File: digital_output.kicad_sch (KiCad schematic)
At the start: 11 parts, among them J4 Conn_01x04_Pin, Q1 NMOS, Q13 PMOS, Q2 NMOS, Q9 PMOS

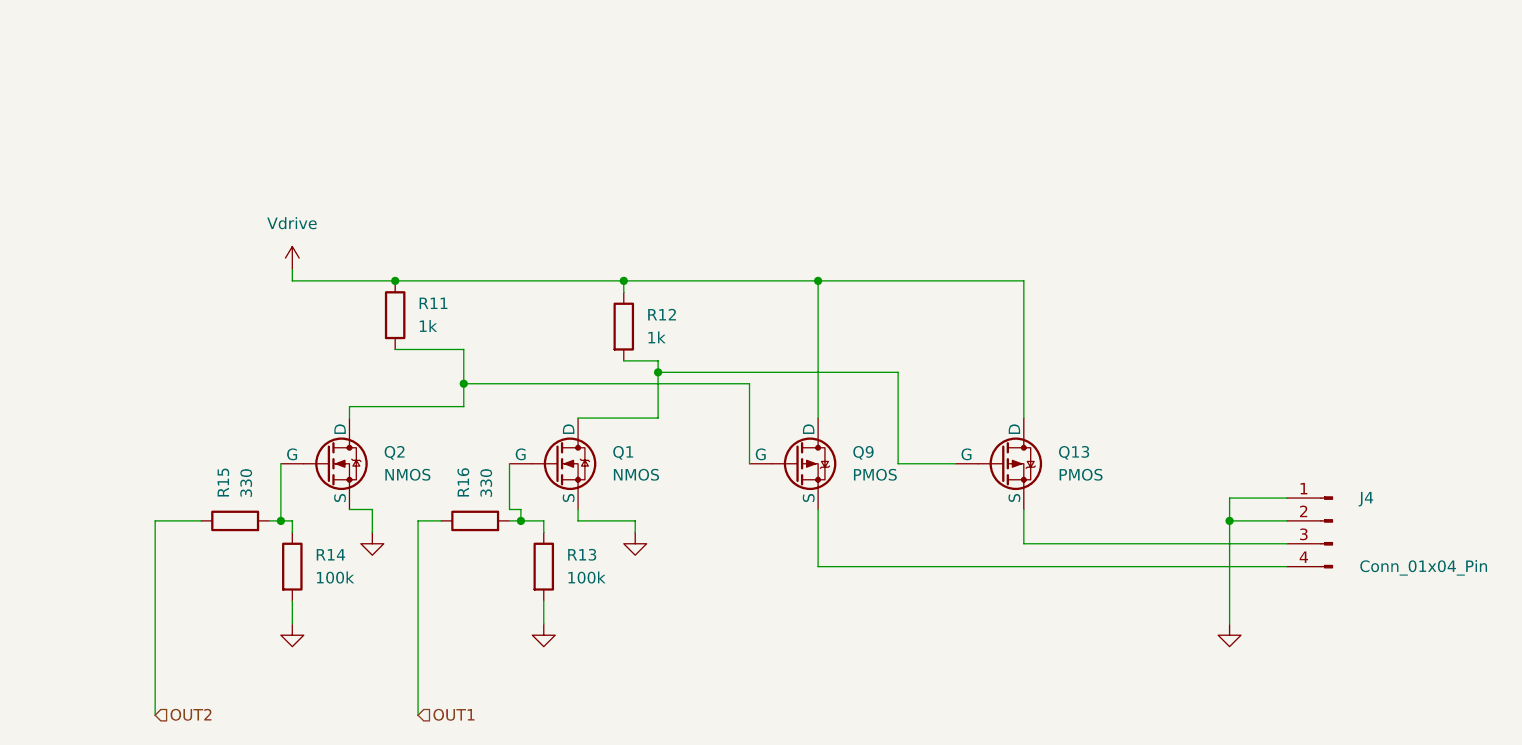
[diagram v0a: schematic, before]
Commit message: cleanup/commenting for better readability, minor corrections
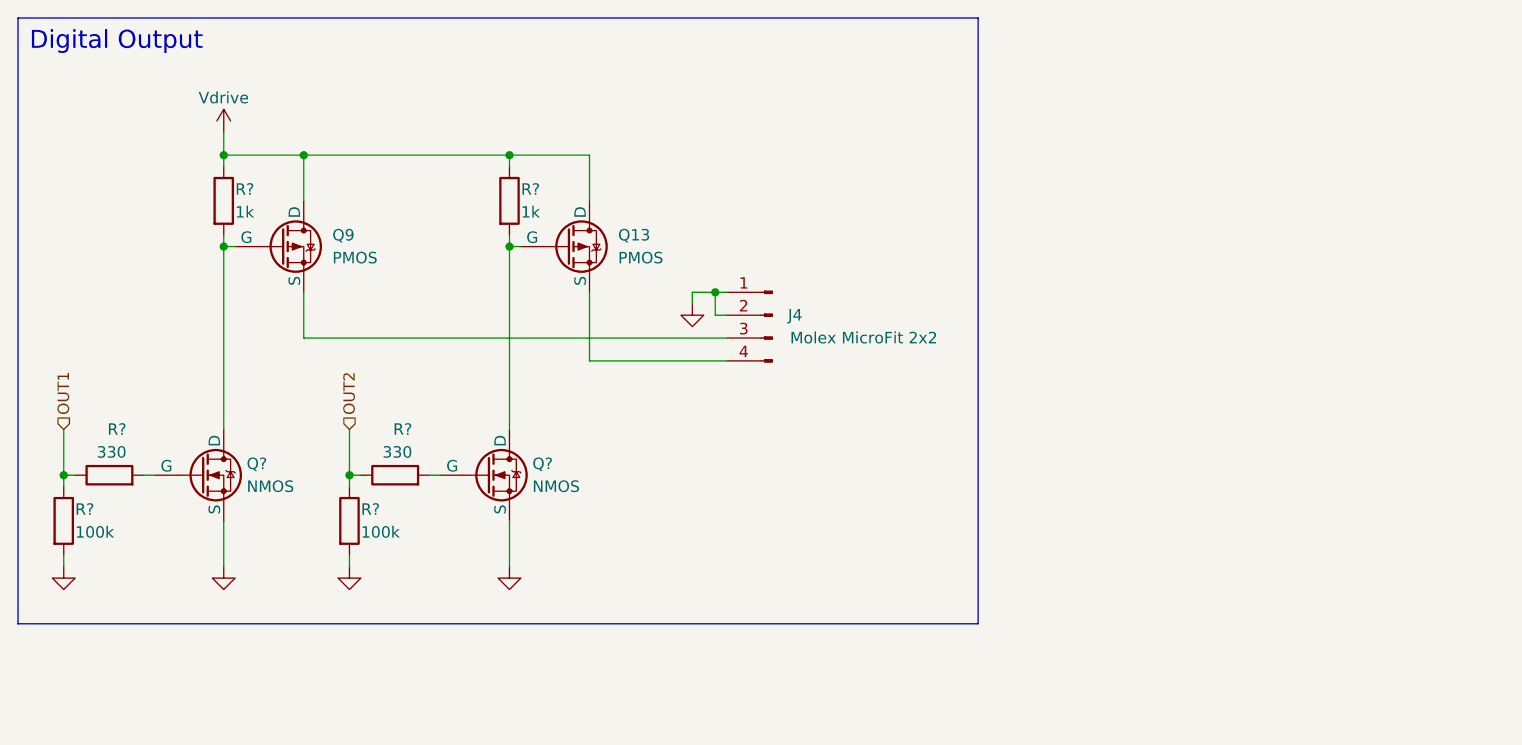
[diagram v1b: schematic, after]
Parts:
- J4: value Conn_01x04_Pin -> Molex MicroFit 2x2
- renumbered Q1 to Q?, Q2 to Q?, R14 to R?, R12 to R?, R11 to R?, R15 to R?, R16 to R?, R13 to R?
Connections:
- net OUT1: now also R?.1, R?.1; no longer R?.1
- net OUT2: now also R?.1, R?.1; no longer R?.1
- net at Q?.2 (G), R?.2: no longer R?.1 (x2)
- net at Q9.3 (S): now also J4.3 (Pin_3); no longer J4.4 (Pin_4)
- net at Q13.3 (S): now also J4.4 (Pin_4); no longer J4.3 (Pin_3)
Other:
- note added: "Digital Output"
- moved on the sheet: J4, Q13, Q9, Q?, R?

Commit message: Add I2C pull-up resistors and digital output flyback diodes
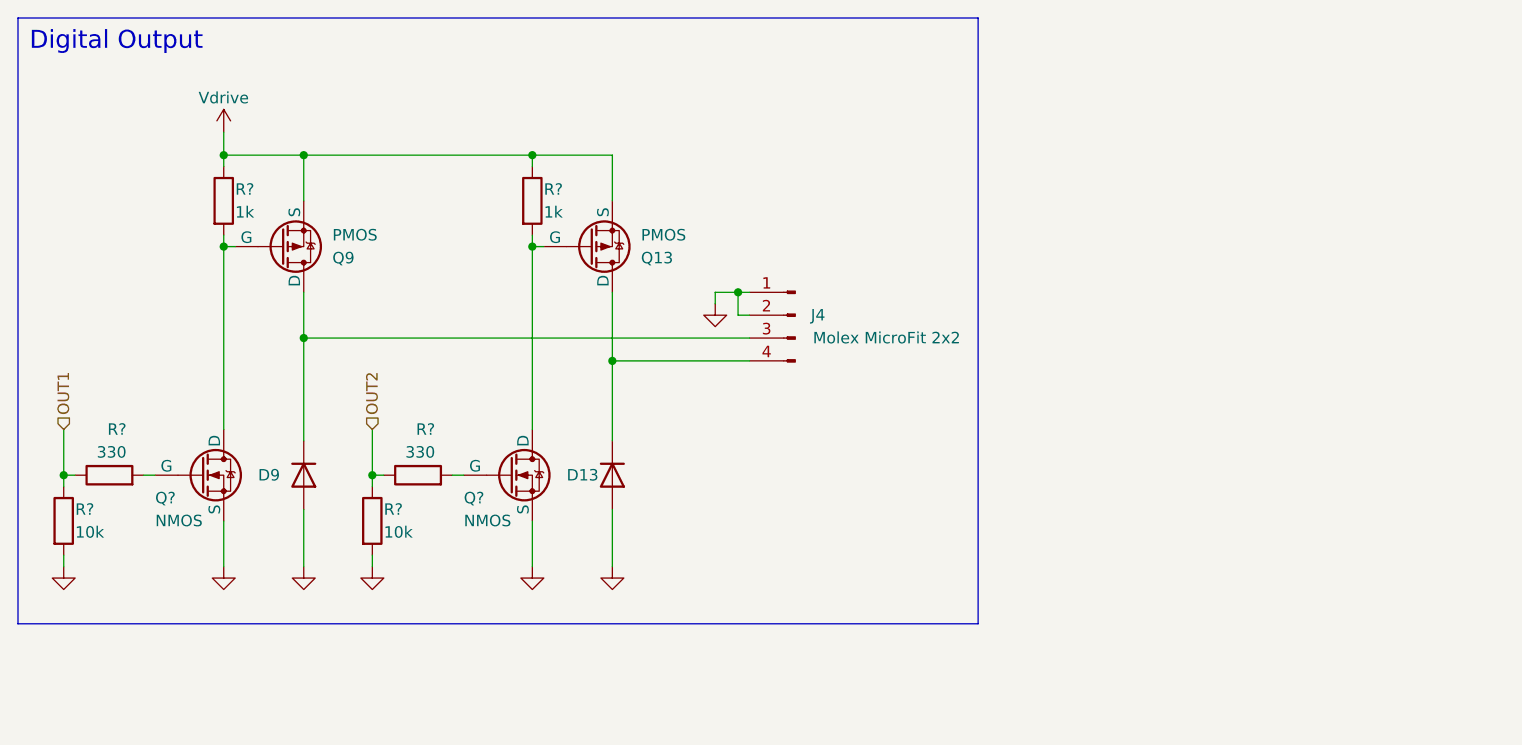
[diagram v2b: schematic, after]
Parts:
- added D13, D9: D, symbol Device:D
- R? (x2): value 100k -> 10k
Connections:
- net GND: now also D13.2 (A), D9.2 (A)
- net Vdrive: now also Q13.3 (S), Q9.3 (S); no longer Q13.1 (D), Q9.1 (D)
- net at J4.3 (Pin_3): now also Q9.1 (D), D9.1 (K); no longer Q9.3 (S)
- net at J4.4 (Pin_4): now also Q13.1 (D), D13.1 (K); no longer Q13.3 (S)
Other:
- moved on the sheet: J4, Q13, Q?, R?

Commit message: Finish footprint assignment
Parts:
- D13, D9: footprint (none) -> Diode_SMD:D_SOD-123F
- J4: footprint (none) -> Connector_Molex:Molex_Micro-Fit_3.0_43045-0400_2x02_P3.00mm_Horizontal
- Q13, Q9, Q? (x2): footprint (none) -> Package_TO_SOT_SMD:SOT-23
- R? (x6): footprint (none) -> Resistor_SMD:R_0603_1608Metric_Pad0.98x0.95mm_HandSolder
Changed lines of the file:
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@@
       (effects (font (size 1.27 1.27)) (justify left))
     )
-    (property "Footprint" "" (at 17.272 69.85 90)
+    (property "Footprint" "Resistor_SMD:R_0603_1608Metric_Pad0.98x0.95mm_HandSolder" (at 17.272 69.85 90)
       (effects (font (size 1.27 1.27)) hide)
     )
@@
       (effects (font (size 1.27 1.27)) (justify left))
     )
-    (property "Footprint" "" (at 73.66 62.23 0)
+    (property "Footprint" "Package_TO_SOT_SMD:SOT-23" (at 73.66 62.23 0)
       (effects (font (size 1.27 1.27)) hide)
     )
@@
       (effects (font (size 1.27 1.27)) (justify left))
     )
-    (property "Footprint" "" (at 69.342 34.29 90)
+    (property "Footprint" "Resistor_SMD:R_0603_1608Metric_Pad0.98x0.95mm_HandSolder" (at 69.342 34.29 90)
       (effects (font (size 1.27 1.27)) hide)
     )
@@
       (effects (font (size 1.27 1.27)) (justify left))
     )
-    (property "Footprint" "" (at 35.052 34.29 90)
+    (property "Footprint" "Resistor_SMD:R_0603_1608Metric_Pad0.98x0.95mm_HandSolder" (at 35.052 34.29 90)
       (effects (font (size 1.27 1.27)) hide)
     )
@@
       (effects (font (size 1.27 1.27)) (justify left))
     )
-    (property "Footprint" "" (at 24.13 66.548 90)
+    (property "Footprint" "Resistor_SMD:R_0603_1608Metric_Pad0.98x0.95mm_HandSolder" (at 24.13 66.548 90)
       (effects (font (size 1.27 1.27)) hide)
     )
@@
       (effects (font (size 1.27 1.27)) (justify left) hide)
     )
-    (property "Footprint" "" (at 80.01 64.77 0)
+    (property "Footprint" "Diode_SMD:D_SOD-123F" (at 80.01 64.77 0)
       (effects (font (size 1.27 1.27)) hide)
     )
@@
       (effects (font (size 1.27 1.27)) (justify left))
     )
-    (property "Footprint" "" (at 48.26 41.91 0)
+    (property "Footprint" "Package_TO_SOT_SMD:SOT-23" (at 48.26 41.91 0)
       (effects (font (size 1.27 1.27)) hide)
     )
@@
       (effects (font (size 1.27 1.27)) (justify left) hide)
     )
-    (property "Footprint" "" (at 45.72 64.77 0)
+    (property "Footprint" "Diode_SMD:D_SOD-123F" (at 45.72 64.77 0)
       (effects (font (size 1.27 1.27)) hide)
     )
@@
       (effects (font (size 1.27 1.27)) (justify left))
     )
-    (property "Footprint" "" (at 58.42 66.548 90)
+    (property "Footprint" "Resistor_SMD:R_0603_1608Metric_Pad0.98x0.95mm_HandSolder" (at 58.42 66.548 90)
       (effects (font (size 1.27 1.27)) hide)
     )
@@
       (effects (font (size 1.27 1.27)) (justify left))
     )
-    (property "Footprint" "" (at 39.37 62.23 0)
+    (property "Footprint" "Package_TO_SOT_SMD:SOT-23" (at 39.37 62.23 0)
       (effects (font (size 1.27 1.27)) hide)
     )
@@
       (effects (font (size 1.27 1.27)) (justify left))
     )
-    (property "Footprint" "" (at 51.562 69.85 90)
+    (property "Footprint" "Resistor_SMD:R_0603_1608Metric_Pad0.98x0.95mm_HandSolder" (at 51.562 69.85 90)
       (effects (font (size 1.27 1.27)) hide)
     )
@@
       (effects (font (size 1.27 1.27)) (justify left))
     )
-    (property "Footprint" "" (at 82.55 41.91 0)
+    (property "Footprint" "Package_TO_SOT_SMD:SOT-23" (at 82.55 41.91 0)
       (effects (font (size 1.27 1.27)) hide)
     )
@@
       (effects (font (size 1.27 1.27)))
     )
-    (property "Footprint" "" (at 100.33 46.99 0)
-      (effects (font (size 1.27 1.27)) hide)
-    )
+    (property "Footprint" "Connector_Molex:Molex_Micro-Fit_3.0_43045-0400_2x02_P3.00mm_Horizontal" (at 100.33 46.99 0)
+      (effects (font (size 1.27 1.27)) hide)
+    )
